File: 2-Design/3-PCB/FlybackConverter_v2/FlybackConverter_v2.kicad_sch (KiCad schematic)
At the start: 55 parts, among them U1 TL431DBV, U2 LM7812_TO220

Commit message: Small updates & 3D models added, tracks to be placed.
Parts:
- INPUT1, OUTPUT1: footprint TerminalBlock_Phoenix:TerminalBlock_Phoenix_MKDS-1,5-2-5.08_1x02_P5.08mm_Horizontal -> kutup:sevgi_konnektosu
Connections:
- net GND1 renamed GNDREF
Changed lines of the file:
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@@
     (effects (font (size 1.27 1.27)) (justify left bottom))
+  )
+  (symbol (lib_id "power:GNDREF") (at 147.32 138.43 0) (unit 1)
+    (in_bom yes) (on_board yes) (fields_autoplaced)
+    (property "Reference" "#PWR0110" (id 0) (at 147.32 144.78 0)
+      (effects (font (size 1.27 1.27)) hide)
+    )
+    (property "Value" "GNDREF" (id 1) (at 147.32 143.51 0))
+    (property "Footprint" "" (id 2) (at 147.32 138.43 0)
+      (effects (font (size 1.27 1.27)) hide)
+    )
+    (property "Datasheet" "" (id 3) (at 147.32 138.43 0)
+      (effects (font (size 1.27 1.27)) hide)
+    )
+    (pin "1")
   )
   (symbol (lib_id "Device:C") (at 134.62 43.18 0) (unit 1)
@@
     (property "Reference" "OUTPUT1" (id 0) (at 271.145 43.18 0))
     (property "Value" "Conn_01x02_Female" (id 1) (at 271.145 45.72 0))
-    (property "Footprint" "TerminalBlock_Phoenix:TerminalBlock_Phoenix_MKDS-1,5-2-5.08_1x02_P5.08mm_Horizontal" (id 2) (at 271.78 50.8 0)
+    (property "Footprint" "kutup:sevgi_konnektosu" (id 2) (at 271.78 50.8 0)
       (effects (font (size 1.27 1.27)) hide)
     )
@@
     (property "Reference" "INPUT1" (id 0) (at 98.425 33.02 0))
     (property "Value" "Conn_01x02_Female" (id 1) (at 98.425 35.56 0))
-    (property "Footprint" "TerminalBlock_Phoenix:TerminalBlock_Phoenix_MKDS-1,5-2-5.08_1x02_P5.08mm_Horizontal" (id 2) (at 97.79 40.64 0)
+    (property "Footprint" "kutup:sevgi_konnektosu" (id 2) (at 97.79 40.64 0)
       (effects (font (size 1.27 1.27)) hide)
     )
@@
     (pin "2")
   )
+  (symbol (lib_id "power:GNDREF") (at 154.94 138.43 0) (unit 1)
+    (in_bom yes) (on_board yes) (fields_autoplaced)
+    (property "Reference" "#PWR0109" (id 0) (at 154.94 144.78 0)
+      (effects (font (size 1.27 1.27)) hide)
+    )
+    (property "Value" "GNDREF" (id 1) (at 154.94 143.51 0))
+    (property "Footprint" "" (id 2) (at 154.94 138.43 0)
+      (effects (font (size 1.27 1.27)) hide)
+    )
+    (property "Datasheet" "" (id 3) (at 154.94 138.43 0)
+      (effects (font (size 1.27 1.27)) hide)
+    )
+    (pin "1")
+  )
   (symbol (lib_id "Device:R") (at 161.29 74.93 90) (unit 1)
     (in_bom yes) (on_board yes) (fields_autoplaced)
@@
     )
     (property "Datasheet" "" (id 3) (at 115.57 88.9 0)
-      (effects (font (size 1.27 1.27)) hide)
-    )
-    (pin "1")
-  )
-  (symbol (lib_id "power:GND1") (at 246.38 54.61 0) (unit 1)
-    (in_bom yes) (on_board yes) (fields_autoplaced)
-    (property "Reference" "#PWR0115" (id 0) (at 246.38 60.96 0)
-      (effects (font (size 1.27 1.27)) hide)
-    )
-    (property "Value" "GND1" (id 1) (at 246.38 59.69 0))
-    (property "Footprint" "" (id 2) (at 246.38 54.61 0)
-      (effects (font (size 1.27 1.27)) hide)
-    )
-    (property "Datasheet" "" (id 3) (at 246.38 54.61 0)
       (effects (font (size 1.27 1.27)) hide)
     )
@@
     (pin "2")
   )
+  (symbol (lib_id "power:GNDREF") (at 207.01 138.43 0) (unit 1)
+    (in_bom yes) (on_board yes) (fields_autoplaced)
+    (property "Reference" "#PWR0108" (id 0) (at 207.01 144.78 0)
+      (effects (font (size 1.27 1.27)) hide)
+    )
+    (property "Value" "GNDREF" (id 1) (at 207.01 143.51 0))
+    (property "Footprint" "" (id 2) (at 207.01 138.43 0)
+      (effects (font (size 1.27 1.27)) hide)
+    )
+    (property "Datasheet" "" (id 3) (at 207.01 138.43 0)
+      (effects (font (size 1.27 1.27)) hide)
+    )
+    (pin "1")
+  )
   (symbol (lib_id "Device:C") (at 123.19 82.55 90) (unit 1)
     (in_bom yes) (on_board yes)
@@
     (pin "2")
   )
-  (symbol (lib_id "power:GND1") (at 207.01 138.43 0) (unit 1)
-    (in_bom yes) (on_board yes) (fields_autoplaced)
-    (property "Reference" "#PWR0110" (id 0) (at 207.01 144.78 0)
-      (effects (font (size 1.27 1.27)) hide)
-    )
-    (property "Value" "GND1" (id 1) (at 207.01 143.51 0))
-    (property "Footprint" "" (id 2) (at 207.01 138.43 0)
-      (effects (font (size 1.27 1.27)) hide)
-    )
-    (property "Datasheet" "" (id 3) (at 207.01 138.43 0)
-      (effects (font (size 1.27 1.27)) hide)
-    )
-    (pin "1")
-  )
   (symbol (lib_id "power:GND") (at 99.06 137.16 0) (unit 1)
     (in_bom yes) (on_board yes) (fields_autoplaced)
@@
     (pin "8")
   )
-  (symbol (lib_id "power:GND1") (at 154.94 138.43 0) (unit 1)
-    (in_bom yes) (on_board yes) (fields_autoplaced)
-    (property "Reference" "#PWR0109" (id 0) (at 154.94 144.78 0)
-      (effects (font (size 1.27 1.27)) hide)
-    )
-    (property "Value" "GND1" (id 1) (at 154.94 143.51 0))
-    (property "Footprint" "" (id 2) (at 154.94 138.43 0)
-      (effects (font (size 1.27 1.27)) hide)
-    )
-    (property "Datasheet" "" (id 3) (at 154.94 138.43 0)
-      (effects (font (size 1.27 1.27)) hide)
-    )
-    (pin "1")
-  )
   (symbol (lib_id "Device:R") (at 207.01 69.85 0) (unit 1)
     (in_bom yes) (on_board yes) (fields_autoplaced)
@@
     (pin "1")
     (pin "2")
+  )
+  (symbol (lib_id "power:GNDREF") (at 246.38 54.61 0) (unit 1)
+    (in_bom yes) (on_board yes) (fields_autoplaced)
+    (property "Reference" "#PWR0114" (id 0) (at 246.38 60.96 0)
+      (effects (font (size 1.27 1.27)) hide)
+    )
+    (property "Value" "GNDREF" (id 1) (at 246.38 59.69 0))
+    (property "Footprint" "" (id 2) (at 246.38 54.61 0)
+      (effects (font (size 1.27 1.27)) hide)
+    )
+    (property "Datasheet" "" (id 3) (at 246.38 54.61 0)
+      (effects (font (size 1.27 1.27)) hide)
+    )
+    (pin "1")
   )
   (symbol (lib_id "Device:C") (at 153.67 80.01 0) (unit 1)
@@
     (pin "2")
   )
-  (symbol (lib_id "power:GND1") (at 147.32 138.43 0) (unit 1)
-    (in_bom yes) (on_board yes) (fields_autoplaced)
-    (property "Reference" "#PWR0108" (id 0) (at 147.32 144.78 0)
-      (effects (font (size 1.27 1.27)) hide)
-    )
-    (property "Value" "GND1" (id 1) (at 147.32 143.51 0))
-    (property "Footprint" "" (id 2) (at 147.32 138.43 0)
-      (effects (font (size 1.27 1.27)) hide)
-    )
-    (property "Datasheet" "" (id 3) (at 147.32 138.43 0)
-      (effects (font (size 1.27 1.27)) hide)
-    )
-    (pin "1")
-  )
   (symbol (lib_id "power:GND") (at 77.47 88.9 0) (unit 1)
     (in_bom yes) (on_board yes) (fields_autoplaced)
@@
       (reference "#PWR0107") (unit 1) (value "GND") (footprint "")
     )
-    (path "/f38c91ce-8869-4340-82dd-ec4dbbcfcefd"
-      (reference "#PWR0108") (unit 1) (value "GND1") (footprint "")
-    )
-    (path "/d08e0a71-5c64-442c-9493-a3a9c39dfb35"
-      (reference "#PWR0109") (unit 1) (value "GND1") (footprint "")
-    )
-    (path "/be60134d-2c42-4d83-84e8-b07ff7bcb5ba"
-      (reference "#PWR0110") (unit 1) (value "GND1") (footprint "")
+    (path "/9bd02831-713c-4a54-97da-8cb516caf612"
+      (reference "#PWR0108") (unit 1) (value "GNDREF") (footprint "")
+    )
+    (path "/60830c8c-12bd-4a10-b4b4-5d599d1b7e62"
+      (reference "#PWR0109") (unit 1) (value "GNDREF") (footprint "")
+    )
+    (path "/03daa3b8-96aa-47ce-880d-5fda0e15f557"
+      (reference "#PWR0110") (unit 1) (value "GNDREF") (footprint "")
     )
     (path "/ca1e513f-c01c-4f93-a3ab-ba78e18c2431"
@@
       (reference "#PWR0113") (unit 1) (value "GND") (footprint "")
     )
-    (path "/8516dc0e-3586-40cd-9dde-6aec3044d1d3"
-      (reference "#PWR0115") (unit 1) (value "GND1") (footprint "")
+    (path "/d74b45e7-f27d-4fc8-b1a6-f46d42645021"
+      (reference "#PWR0114") (unit 1) (value "GNDREF") (footprint "")
     )
     (path "/4a1f52f6-40bf-4f2a-9ea0-c63673a0a41c"
@@
     )
     (path "/5218f09f-4a8c-4246-bbc5-dc5a647f8801"
-      (reference "INPUT1") (unit 1) (value "Conn_01x02_Female") (footprint "TerminalBlock_Phoenix:TerminalBlock_Phoenix_MKDS-1,5-2-5.08_1x02_P5.08mm_Horizontal")
+      (reference "INPUT1") (unit 1) (value "Conn_01x02_Female") (footprint "kutup:sevgi_konnektosu")
     )
     (path "/4172f9f5-af9c-467d-8404-d5682f0fee29"
@@
     )
     (path "/487a895f-4c3d-4c29-a9ff-8cf89ba54c09"
-      (reference "OUTPUT1") (unit 1) (value "Conn_01x02_Female") (footprint "TerminalBlock_Phoenix:TerminalBlock_Phoenix_MKDS-1,5-2-5.08_1x02_P5.08mm_Horizontal")
+      (reference "OUTPUT1") (unit 1) (value "Conn_01x02_Female") (footprint "kutup:sevgi_konnektosu")
     )
     (path "/9117228d-0af7-4715-ab37-bc92df2921d5"

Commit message: Tracks around the damn IC are almost done.
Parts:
- DC1: footprint Diode_SMD:D_SOD-523 -> Diode_SMD:D_SOD-123
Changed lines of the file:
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@@
       (effects (font (size 1.27 1.27)) (justify left))
     )
-    (property "Footprint" "Diode_SMD:D_SOD-523" (id 2) (at 202.565 120.65 0)
+    (property "Footprint" "Diode_SMD:D_SOD-123" (id 2) (at 202.565 120.65 0)
       (effects (font (size 1.27 1.27)) hide)
     )
@@
     )
     (path "/14c7ef54-cc8d-4e3a-aea4-32382626f4f7"
-      (reference "DC1") (unit 1) (value "DZ2S100X0L") (footprint "Diode_SMD:D_SOD-523")
+      (reference "DC1") (unit 1) (value "DZ2S100X0L") (footprint "Diode_SMD:D_SOD-123")
     )
     (path "/e6040600-fa22-41e1-a300-9b6e6350445e"

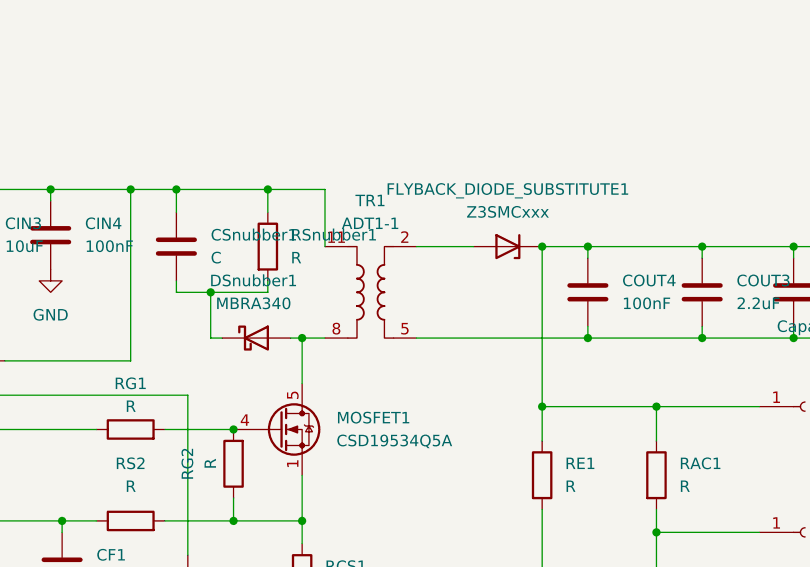
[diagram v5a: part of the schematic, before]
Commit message: Output side tracks almost completed.,
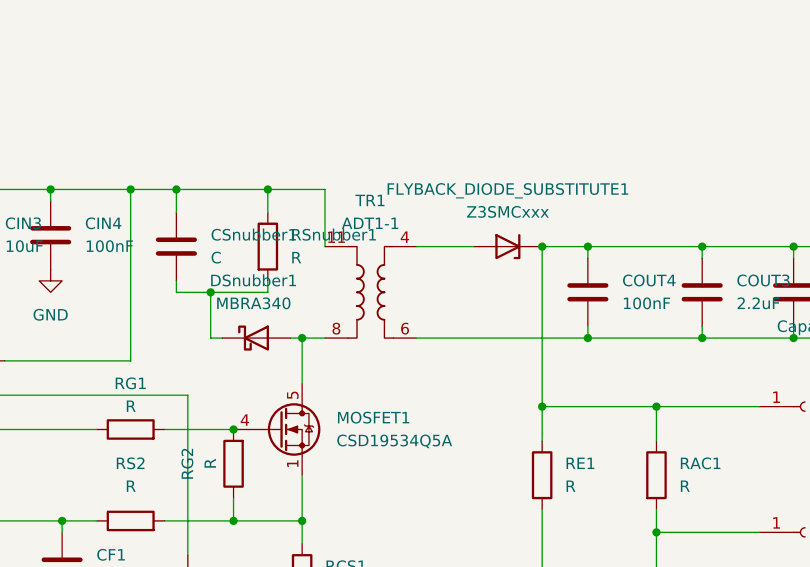
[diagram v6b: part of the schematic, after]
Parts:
- RCS1: footprint Resistor_SMD:R_2010_5025Metric_Pad1.40x2.65mm_HandSolder -> Resistor_SMD:R_1206_3216Metric_Pad1.30x1.75mm_HandSolder
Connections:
- net GNDREF: now also TR1.6; no longer TR1.5
- net at FLYBACK_DIODE_SUBSTITUTE1.2 (A): now also TR1.4 (w~); no longer TR1.2
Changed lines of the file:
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@@
     )
     (pin "11")
-    (pin "2")
-    (pin "5")
+    (pin "4")
+    (pin "6")
     (pin "8")
   )
@@
       (effects (font (size 1.27 1.27)) (justify left))
     )
-    (property "Footprint" "Resistor_SMD:R_2010_5025Metric_Pad1.40x2.65mm_HandSolder" (id 2) (at 178.562 81.28 90)
+    (property "Footprint" "Resistor_SMD:R_1206_3216Metric_Pad1.30x1.75mm_HandSolder" (id 2) (at 178.562 81.28 90)
       (effects (font (size 1.27 1.27)) hide)
     )
@@
     )
     (path "/eda2c49b-e8f6-4fe3-a39b-89b83269e1b8"
-      (reference "RCS1") (unit 1) (value "R") (footprint "Resistor_SMD:R_2010_5025Metric_Pad1.40x2.65mm_HandSolder")
+      (reference "RCS1") (unit 1) (value "R") (footprint "Resistor_SMD:R_1206_3216Metric_Pad1.30x1.75mm_HandSolder")
     )
     (path "/d5eca49d-042c-4463-8ab4-7c004c4938ff"

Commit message: I guess, only last edits left for PCB design.
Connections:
- net GND: now also INPUT1.2 (Pin_2); no longer INPUT1.1 (Pin_1)
- net at CIN1.1, CIN2.1, CIN3.1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: now also INPUT1.1 (Pin_1), TR1.9; no longer INPUT1.2 (Pin_2), TR1.11
- net at DSnubber1.2 (A), MOSFET1.5 (D): now also TR1.7; no longer TR1.8
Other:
- moved on the sheet: INPUT1
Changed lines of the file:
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@@
     (pin "5")
   )
-  (symbol (lib_id "Connector:Conn_01x02_Female") (at 97.79 40.64 180) (unit 1)
+  (symbol (lib_id "Connector:Conn_01x02_Female") (at 97.79 38.1 0) (mirror y) (unit 1)
     (in_bom yes) (on_board yes) (fields_autoplaced)
     (property "Reference" "INPUT1" (id 0) (at 98.425 33.02 0))
     (property "Value" "Conn_01x02_Female" (id 1) (at 98.425 35.56 0))
-    (property "Footprint" "kutup:sevgi_konnektosu" (id 2) (at 97.79 40.64 0)
-      (effects (font (size 1.27 1.27)) hide)
-    )
-    (property "Datasheet" "~" (id 3) (at 97.79 40.64 0)
+    (property "Footprint" "kutup:sevgi_konnektosu" (id 2) (at 97.79 38.1 0)
+      (effects (font (size 1.27 1.27)) hide)
+    )
+    (property "Datasheet" "~" (id 3) (at 97.79 38.1 0)
       (effects (font (size 1.27 1.27)) hide)
     )
@@
       (effects (font (size 1.27 1.27)) hide)
     )
-    (pin "11")
+    (pin "9")
     (pin "4")
     (pin "6")
-    (pin "8")
+    (pin "7")
   )
   (symbol (lib_id "Device:R") (at 207.01 69.85 0) (unit 1)

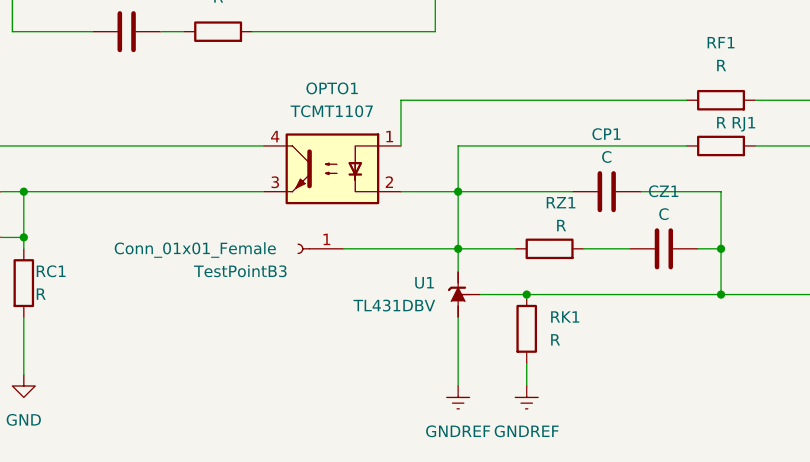
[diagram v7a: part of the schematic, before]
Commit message: Gate loop is too long :'(. I_sense capacitor should also be placed closer to the IC.
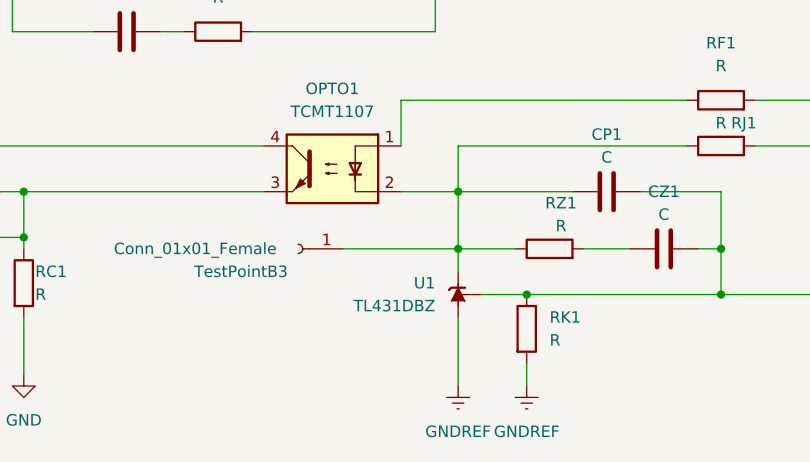
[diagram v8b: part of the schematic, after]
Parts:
- removed U1: TL431DBV, Package_TO_SOT_SMD:SOT-23-5, symbol Reference_Voltage:TL431DBV
- added U1: TL431DBZ, Package_TO_SOT_SMD:SOT-23, symbol Reference_Voltage:TL431DBZ
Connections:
- net GNDREF: now also U1.3 (A)
- net at CP1.2, CZ1.2, RI1.2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: now also U1.2 (REF)
- net at CP1.1, OPTO1.2, RJ1.1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: now also U1.1 (K)
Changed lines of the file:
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@@
+    (stroke (width 0) (type default) (color 0 0 0 0))
+  )
+  (wire (pts (xy 147.32 123.19) (xy 147.32 125.73))
     (stroke (width 0) (type default) (color 0 0 0 0))
   )
@@
   )
   (wire (pts (xy 100.33 72.39) (xy 102.87 72.39))
-    (stroke (width 0) (type default) (color 0 0 0 0))
-  )
-  (wire (pts (xy 147.32 125.73) (xy 147.32 123.19))
     (stroke (width 0) (type default) (color 0 0 0 0))
   )
@@
     (pin "1")
     (pin "2")
-  )
-  (symbol (lib_id "Reference_Voltage:TL431DBV") (at 147.32 128.27 270) (mirror x) (unit 1)
-    (in_bom yes) (on_board yes) (fields_autoplaced)
-    (property "Reference" "U1" (id 0) (at 144.78 126.9999 90)
-      (effects (font (size 1.27 1.27)) (justify right))
-    )
-    (property "Value" "TL431DBV" (id 1) (at 144.78 129.5399 90)
-      (effects (font (size 1.27 1.27)) (justify right))
-    )
-    (property "Footprint" "Package_TO_SOT_SMD:SOT-23-5" (id 2) (at 140.97 128.27 0)
-      (effects (font (size 1.27 1.27) italic) hide)
-    )
-    (property "Datasheet" "http://www.ti.com/lit/ds/symlink/tl431.pdf" (id 3) (at 147.32 128.27 0)
-      (effects (font (size 1.27 1.27) italic) hide)
-    )
-    (pin "3")
-    (pin "4")
-    (pin "5")
   )
   (symbol (lib_id "Connector:Conn_01x02_Female") (at 97.79 38.1 0) (mirror y) (unit 1)
@@
     (pin "2")
   )
+  (symbol (lib_id "Reference_Voltage:TL431DBZ") (at 147.32 128.27 270) (mirror x) (unit 1)
+    (in_bom yes) (on_board yes) (fields_autoplaced)
+    (property "Reference" "U1" (id 0) (at 144.78 126.9999 90)
+      (effects (font (size 1.27 1.27)) (justify right))
+    )
+    (property "Value" "TL431DBZ" (id 1) (at 144.78 129.5399 90)
+      (effects (font (size 1.27 1.27)) (justify right))
+    )
+    (property "Footprint" "Package_TO_SOT_SMD:SOT-23" (id 2) (at 143.51 128.27 0)
+      (effects (font (size 1.27 1.27) italic) hide)
+    )
+    (property "Datasheet" "http://www.ti.com/lit/ds/symlink/tl431.pdf" (id 3) (at 147.32 128.27 0)
+      (effects (font (size 1.27 1.27) italic) hide)
+    )
+    (pin "1")
+    (pin "2")
+    (pin "3")
+  )
   (symbol (lib_id "power:GND") (at 99.06 137.16 0) (unit 1)
     (in_bom yes) (on_board yes) (fields_autoplaced)
@@
       (effects (font (size 1.27 1.27)) hide)
     )
-    (pin "9")
     (pin "4")
     (pin "6")
     (pin "7")
+    (pin "9")
   )
   (symbol (lib_id "Device:R") (at 207.01 69.85 0) (unit 1)
@@
       (reference "TestPointB5") (unit 1) (value "Conn_01x01_Female") (footprint "kutup:TestPoint_THTPad_2.0x2.0mm_Drill1.0mm")
     )
-    (path "/5055a1a2-577c-4ee6-8015-f5357c604648"
-      (reference "U1") (unit 1) (value "TL431DBV") (footprint "Package_TO_SOT_SMD:SOT-23-5")
+    (path "/b1de1fd9-9b87-4e87-bced-9042ad1876a6"
+      (reference "U1") (unit 1) (value "TL431DBZ") (footprint "Package_TO_SOT_SMD:SOT-23")
     )
     (path "/55d61ff5-cee8-4a7b-bbf6-835e09db08f3"
